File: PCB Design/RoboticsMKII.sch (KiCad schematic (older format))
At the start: 0 parts

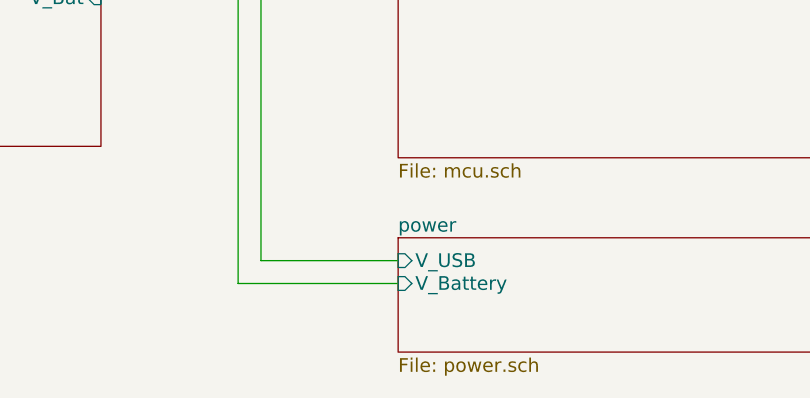
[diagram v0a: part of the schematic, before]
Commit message: Added initial footprint associations, caps and resistors.
Kicad is giving weird errors for the libraries and BOM generator.
The libraries have to be downloaded manually from github, and
then added.

Signed-off-by: Kolijn Wolfaardt <kolijn.wolfaardt@gmail.com>
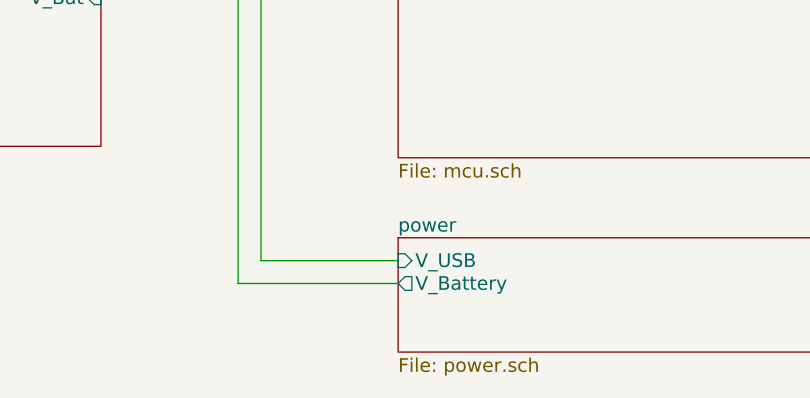
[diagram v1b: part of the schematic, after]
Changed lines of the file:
@@
 F0 "power" 60
 F1 "power.sch" 60
-F2 "V_Battery" I L 4800 5700 60
-F3 "V_USB" I L 4800 5600 60
+F2 "V_USB" I L 4800 5600 60
+F3 "V_Battery" O L 4800 5700 60
 $EndSheet
 $Sheet

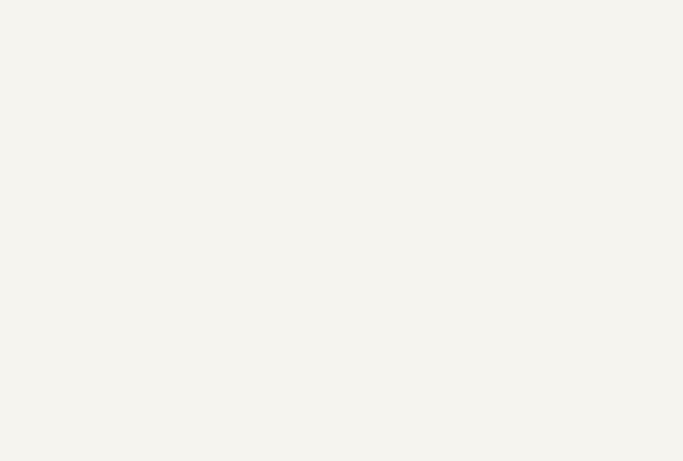
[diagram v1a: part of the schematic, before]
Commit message: Finished the footprint allocation, started on the PCB layout.-s
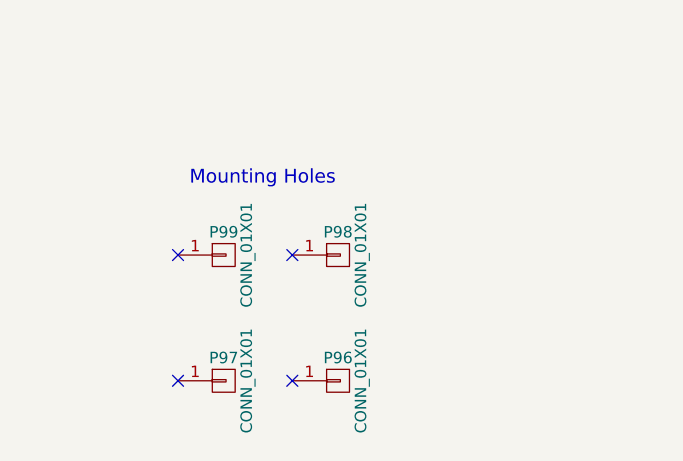
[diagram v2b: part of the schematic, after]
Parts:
- added P96, P97, P98, P99: CONN_01X01, RoBoC:MountingHole3mm, symbol CONN_01X01
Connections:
- no-connect marks 0 -> 4
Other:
- note added: "Mounting Holes"
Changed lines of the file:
@@
 Wire Wire Line
 	4100 4450 3500 4450
+$Comp
+L CONN_01X01 P99
+U 1 1 551B0034
+P 2000 6350
+F 0 "P99" H 2000 6450 50  0000 C CNN
+F 1 "CONN_01X01" V 2100 6350 50  0000 C CNN
+F 2 "RoBoC:MountingHole3mm" H 2000 6350 60  0001 C CNN
+F 3 "" H 2000 6350 60  0000 C CNN
+	1    2000 6350
+	1    0    0    -1
+$EndComp
+$Comp
+L CONN_01X01 P98
+U 1 1 551B0790
+P 2500 6350
+F 0 "P98" H 2500 6450 50  0000 C CNN
+F 1 "CONN_01X01" V 2600 6350 50  0000 C CNN
+F 2 "RoBoC:MountingHole3mm" H 2500 6350 60  0001 C CNN
+F 3 "" H 2500 6350 60  0000 C CNN
+	1    2500 6350
+	1    0    0    -1
+$EndComp
+$Comp
+L CONN_01X01 P96
+U 1 1 551B08EA
+P 2500 6900
+F 0 "P96" H 2500 7000 50  0000 C CNN
+F 1 "CONN_01X01" V 2600 6900 50  0000 C CNN
+F 2 "RoBoC:MountingHole3mm" H 2500 6900 60  0001 C CNN
+F 3 "" H 2500 6900 60  0000 C CNN
+	1    2500 6900
+	1    0    0    -1
+$EndComp
+$Comp
+L CONN_01X01 P97
+U 1 1 551B0A44
+P 2000 6900
+F 0 "P97" H 2000 7000 50  0000 C CNN
+F 1 "CONN_01X01" V 2100 6900 50  0000 C CNN
+F 2 "RoBoC:MountingHole3mm" H 2000 6900 60  0001 C CNN
+F 3 "" H 2000 6900 60  0000 C CNN
+	1    2000 6900
+	1    0    0    -1
+$EndComp
+NoConn ~ 2300 6350
+NoConn ~ 1800 6350
+NoConn ~ 1800 6900
+NoConn ~ 2300 6900
+Text Notes 1850 6050 0    60   ~ 0
+Mounting Holes
 $EndSCHEMATC

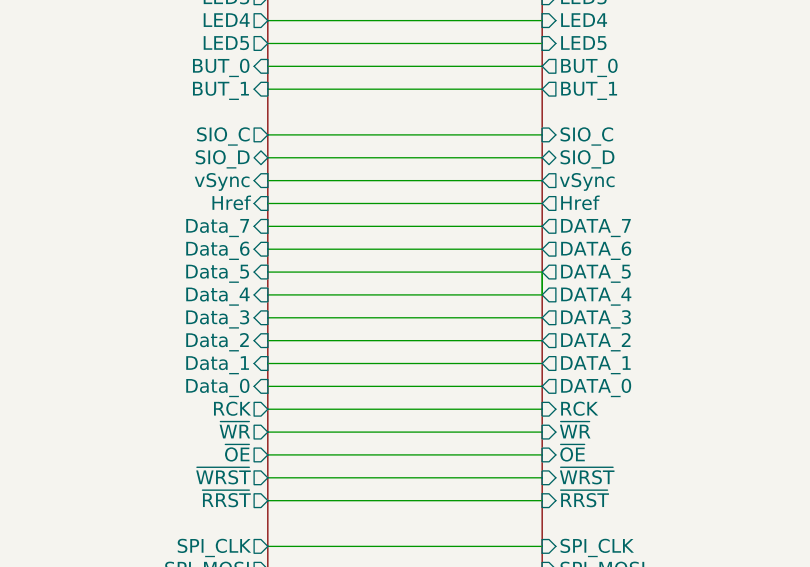
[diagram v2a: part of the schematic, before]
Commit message: Motor Diodes done, some of the power connections
Signed-off-by: Kolijn_Laptop <kolijn.wolfaardt@gmail.com>
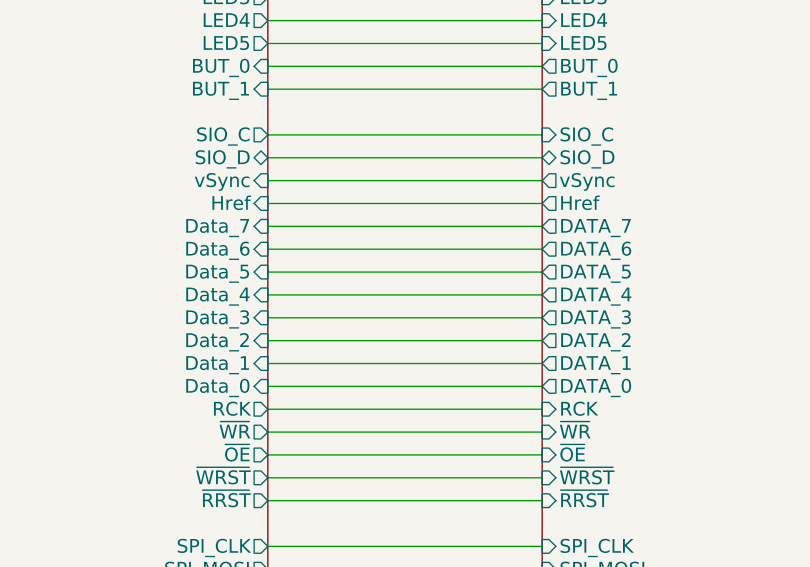
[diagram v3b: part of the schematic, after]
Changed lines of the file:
@@
 F18 "Href" O L 8400 2950 60
 F19 "DATA_7" O L 8400 3050 60
-F20 "DATA_5" O L 8400 3250 60
-F21 "DATA_3" O L 8400 3450 60
-F22 "DATA_1" O L 8400 3650 60
-F23 "DATA_6" O L 8400 3150 60
-F24 "DATA_4" O L 8400 3350 60
-F25 "DATA_2" O L 8400 3550 60
-F26 "DATA_0" O L 8400 3750 60
-F27 "RCK" I L 8400 3850 60
-F28 "~WR" I L 8400 3950 60
-F29 "~OE" I L 8400 4050 60
-F30 "~WRST" I L 8400 4150 60
-F31 "~RRST" I L 8400 4250 60
-F32 "SPI_CLK" I L 8400 4450 60
-F33 "SPI_MOSI" I L 8400 4550 60
-F34 "SPI_MISO" O L 8400 4650 60
-F35 "SPI_SS" I L 8400 4750 60
-F36 "DACOUT" I L 8400 4950 60
-F37 "Reed" I L 8400 5050 60
-F38 "LED5" I L 8400 2250 60
+F20 "DATA_3" O L 8400 3450 60
+F21 "DATA_1" O L 8400 3650 60
+F22 "DATA_6" O L 8400 3150 60
+F23 "DATA_2" O L 8400 3550 60
+F24 "DATA_0" O L 8400 3750 60
+F25 "RCK" I L 8400 3850 60
+F26 "~WR" I L 8400 3950 60
+F27 "~OE" I L 8400 4050 60
+F28 "~WRST" I L 8400 4150 60
+F29 "~RRST" I L 8400 4250 60
+F30 "SPI_CLK" I L 8400 4450 60
+F31 "SPI_MOSI" I L 8400 4550 60
+F32 "SPI_MISO" O L 8400 4650 60
+F33 "SPI_SS" I L 8400 4750 60
+F34 "DACOUT" I L 8400 4950 60
+F35 "Reed" I L 8400 5050 60
+F36 "LED5" I L 8400 2250 60
+F37 "DATA_5" O L 8400 3250 60
+F38 "DATA_4" O L 8400 3350 60
 $EndSheet
 $Sheet
@@
 F30 "Data_7" I R 7200 3050 60
 F31 "Data_6" I R 7200 3150 60
-F32 "Data_5" I R 7200 3250 60
-F33 "Data_4" I R 7200 3350 60
-F34 "Data_3" I R 7200 3450 60
-F35 "Data_2" I R 7200 3550 60
-F36 "Data_1" I R 7200 3650 60
-F37 "Data_0" I R 7200 3750 60
-F38 "BUT_0" I R 7200 2350 60
-F39 "BUT_1" I R 7200 2450 60
-F40 "MOT2_ENC" I L 4800 4250 60
-F41 "MOT1_ENC" I L 4800 3850 60
-F42 "SIO_C" O R 7200 2650 60
-F43 "U1RX" I L 4800 1050 60
-F44 "U1TX" O L 4800 1150 60
-F45 "SERVO_1" O L 4800 3250 60
-F46 "SIO_D" B R 7200 2750 60
-F47 "~OE" O R 7200 4050 60
-F48 "RCK" O R 7200 3850 60
-F49 "LED5" O R 7200 2250 60
-F50 "MOT1_D1" O L 4800 3650 60
+F32 "Data_3" I R 7200 3450 60
+F33 "Data_2" I R 7200 3550 60
+F34 "Data_1" I R 7200 3650 60
+F35 "Data_0" I R 7200 3750 60
+F36 "BUT_0" I R 7200 2350 60
+F37 "BUT_1" I R 7200 2450 60
+F38 "MOT2_ENC" I L 4800 4250 60
+F39 "MOT1_ENC" I L 4800 3850 60
+F40 "SIO_C" O R 7200 2650 60
+F41 "U1RX" I L 4800 1050 60
+F42 "U1TX" O L 4800 1150 60
+F43 "SERVO_1" O L 4800 3250 60
+F44 "SIO_D" B R 7200 2750 60
+F45 "~OE" O R 7200 4050 60
+F46 "RCK" O R 7200 3850 60
+F47 "LED5" O R 7200 2250 60
+F48 "MOT1_D1" O L 4800 3650 60
+F49 "Data_4" I R 7200 3350 60
+F50 "Data_5" I R 7200 3250 60
 $EndSheet
 Wire Wire Line
@@
 Wire Wire Line
 	8400 3150 7200 3150
-Wire Wire Line
-	7200 3250 8400 3250
-Wire Wire Line
-	8400 3250 8400 3350
-Wire Wire Line
-	8400 3350 7200 3350
 Wire Wire Line
 	8400 3450 7200 3450
@@
 Text Notes 1850 6050 0    60   ~ 0
 Mounting Holes
+Wire Wire Line
+	8400 3250 7200 3250
+Wire Wire Line
+	7200 3350 8400 3350
 $EndSCHEMATC
